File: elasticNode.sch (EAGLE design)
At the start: 136 parts, among them J1 FEMALE_HEADER_2X1, J2 JUMPER, J3 JUMPER, J5 FEMALE_HEADER_10X2, J6 USB_CONNMICRO_SMT, J7 USB_CONNMICRO_SMT, M1 SISS23DN, M2 SISS23DN, M3 SISS23DN, M4 SISS23DN, U1 AT90USB128, U10 LTC3419DFN, U11 PAC1720, U14 LTC3419DFN, U2 IS66WV51216EALL, U3 MRF24J40MA, U4 SPARTAN7-LX15, U5 ATMEGA32U4QFN, U6 SST26VF032BWDFN, U7 PAC1720, U8 PAC1720, U9 PAC1720, X1 8MHz, X2 50MHz, X3 32MHz, X4 100MHz, X5 8MHz

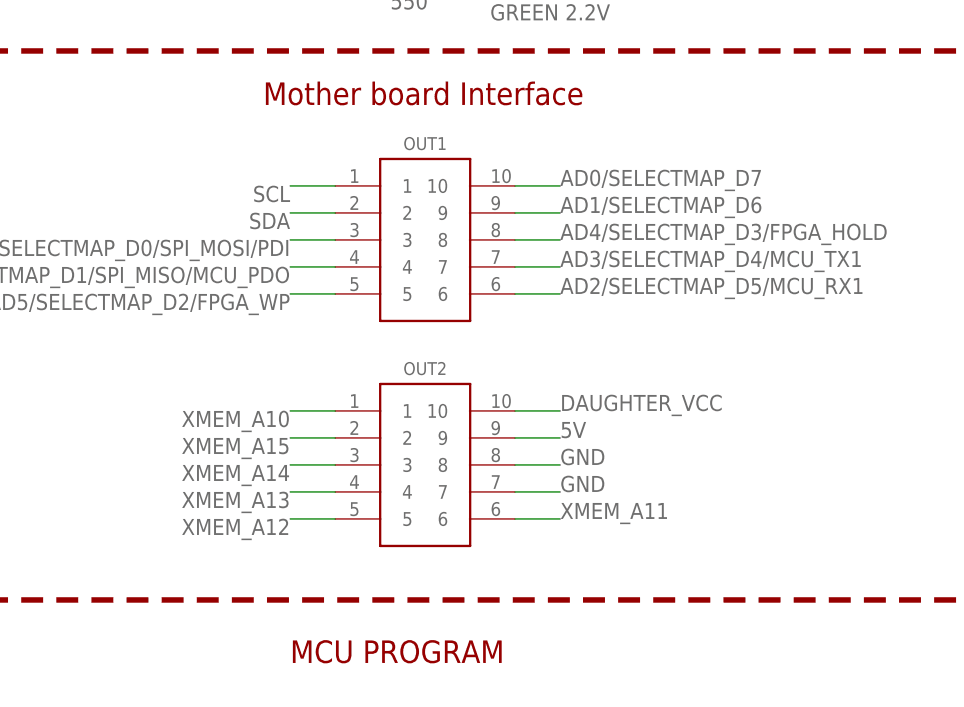
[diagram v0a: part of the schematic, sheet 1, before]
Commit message: Fixed all  DRC Errors and Warnings.
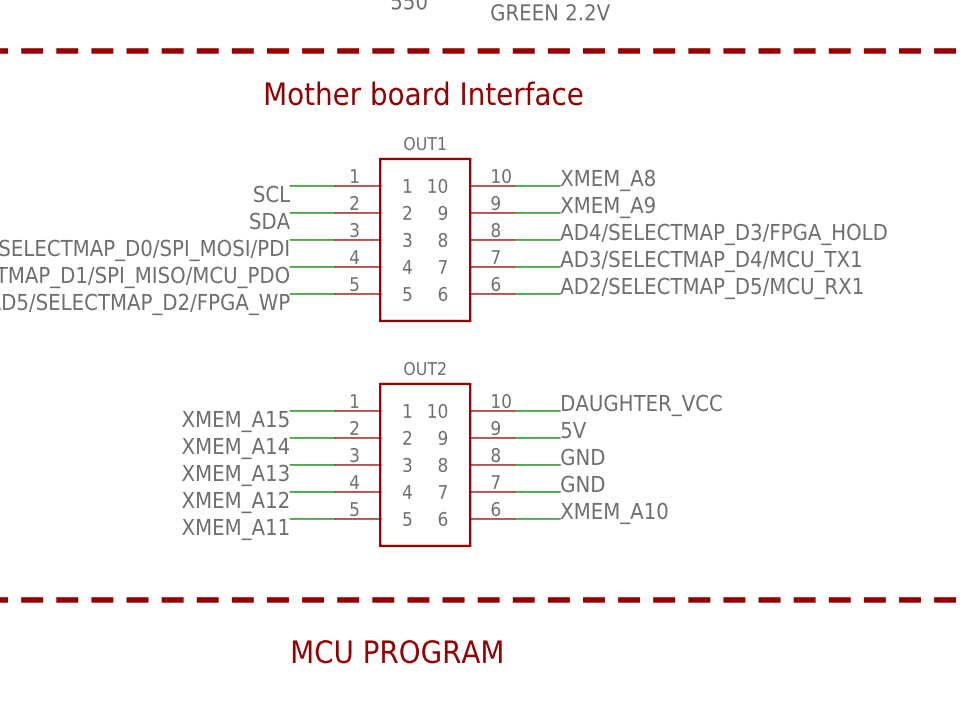
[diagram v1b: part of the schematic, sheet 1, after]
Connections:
- net AD0/SELECTMAP_D7: no longer OUT1.10
- net AD1/SELECTMAP_D6: no longer OUT1.9
- net XMEM_A10: now also OUT2.6; no longer OUT2.1
- net XMEM_A11: now also OUT2.5; no longer OUT2.6
- net XMEM_A12: now also OUT2.4; no longer OUT2.5
- net XMEM_A13: now also OUT2.3; no longer OUT2.4
- net XMEM_A14: now also OUT2.2; no longer OUT2.3
- net XMEM_A15: now also OUT2.1; no longer OUT2.2
- net XMEM_A8: now also OUT1.10
- net XMEM_A9: now also OUT1.9
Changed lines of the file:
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@@
 <setting verticaltext="up"/>
 </settings>
-<grid distance="1" unitdist="mm" unit="mm" style="lines" multiple="1" display="yes" altdistance="0.01" altunitdist="inch" altunit="inch"/>
+<grid distance="0.1" unitdist="inch" unit="inch" style="lines" multiple="1" display="no" altdistance="0.01" altunitdist="inch" altunit="inch"/>
 <layers>
 <layer number="1" name="Top" color="12" fill="1" visible="no" active="no"/>
@@
 <label x="-52" y="67" size="1.778" layer="95" rot="R90"/>
 </segment>
-<segment>
-<pinref part="OUT1" gate="G$1" pin="9"/>
-<wire x1="132" y1="43" x2="137" y2="43" width="0.1524" layer="91"/>
-<label x="137" y="43" size="1.778" layer="95"/>
-</segment>
 </net>
 <net name="AD3/SELECTMAP_D4/MCU_TX1" class="0">
@@
 </segment>
 <segment>
-<pinref part="OUT2" gate="G$1" pin="2"/>
-<wire x1="112" y1="18" x2="107" y2="18" width="0.1524" layer="91"/>
-<label x="107" y="18" size="1.778" layer="95" rot="R180"/>
+<pinref part="OUT2" gate="G$1" pin="1"/>
+<wire x1="112" y1="21" x2="107" y2="21" width="0.1524" layer="91"/>
+<label x="107" y="21" size="1.778" layer="95" rot="R180"/>
 </segment>
 </net>
@@
 <wire x1="-55" y1="51.16" x2="-55" y2="67" width="0.1524" layer="91"/>
 <label x="-55" y="67" size="1.778" layer="95" rot="R90"/>
-</segment>
-<segment>
-<pinref part="OUT1" gate="G$1" pin="10"/>
-<wire x1="132" y1="46" x2="137" y2="46" width="0.1524" layer="91"/>
-<label x="137" y="46" size="1.778" layer="95"/>
 </segment>
 </net>
@@
 <label x="-13" y="-10" size="1.778" layer="95"/>
 </segment>
+<segment>
+<pinref part="OUT1" gate="G$1" pin="10"/>
+<wire x1="132" y1="46" x2="137" y2="46" width="0.1524" layer="91"/>
+<label x="137" y="46" size="1.778" layer="95"/>
+</segment>
 </net>
 <net name="XMEM_A14" class="0">
@@
 </segment>
 <segment>
+<pinref part="OUT2" gate="G$1" pin="2"/>
+<wire x1="112" y1="18" x2="107" y2="18" width="0.1524" layer="91"/>
+<label x="107" y="18" size="1.778" layer="95" rot="R180"/>
+</segment>
+</net>
+<net name="XMEM_A13" class="0">
+<segment>
+<pinref part="U1" gate="G$1" pin="PC5(A13/OC.3B)"/>
+<wire x1="-26" y1="5" x2="-13" y2="5" width="0.1524" layer="91"/>
+<label x="-13" y="5" size="1.778" layer="95"/>
+</segment>
+<segment>
 <pinref part="OUT2" gate="G$1" pin="3"/>
 <wire x1="112" y1="15" x2="107" y2="15" width="0.1524" layer="91"/>
@@
 </segment>
 </net>
-<net name="XMEM_A13" class="0">
-<segment>
-<pinref part="U1" gate="G$1" pin="PC5(A13/OC.3B)"/>
-<wire x1="-26" y1="5" x2="-13" y2="5" width="0.1524" layer="91"/>
-<label x="-13" y="5" size="1.778" layer="95"/>
+<net name="XMEM_A12" class="0">
+<segment>
+<pinref part="U1" gate="G$1" pin="PC4(A12/OC.3C)"/>
+<wire x1="-26" y1="2" x2="-13" y2="2" width="0.1524" layer="91"/>
+<label x="-13" y="2" size="1.778" layer="95"/>
 </segment>
 <segment>
@@
 </segment>
 </net>
-<net name="XMEM_A12" class="0">
-<segment>
-<pinref part="U1" gate="G$1" pin="PC4(A12/OC.3C)"/>
-<wire x1="-26" y1="2" x2="-13" y2="2" width="0.1524" layer="91"/>
-<label x="-13" y="2" size="1.778" layer="95"/>
+<net name="XMEM_A11" class="0">
+<segment>
+<pinref part="U1" gate="G$1" pin="PC3(A11/T.3)"/>
+<wire x1="-26" y1="-1" x2="-13" y2="-1" width="0.1524" layer="91"/>
+<label x="-13" y="-1" size="1.778" layer="95"/>
 </segment>
 <segment>
@@
 </segment>
 </net>
-<net name="XMEM_A11" class="0">
-<segment>
-<pinref part="U1" gate="G$1" pin="PC3(A11/T.3)"/>
-<wire x1="-26" y1="-1" x2="-13" y2="-1" width="0.1524" layer="91"/>
-<label x="-13" y="-1" size="1.778" layer="95"/>
+<net name="XMEM_A10" class="0">
+<segment>
+<pinref part="U1" gate="G$1" pin="PC2(A10)"/>
+<wire x1="-26" y1="-4" x2="-13" y2="-4" width="0.1524" layer="91"/>
+<label x="-13" y="-4" size="1.778" layer="95"/>
 </segment>
 <segment>
@@
 </segment>
 </net>
-<net name="XMEM_A10" class="0">
-<segment>
-<pinref part="U1" gate="G$1" pin="PC2(A10)"/>
-<wire x1="-26" y1="-4" x2="-13" y2="-4" width="0.1524" layer="91"/>
-<label x="-13" y="-4" size="1.778" layer="95"/>
-</segment>
-<segment>
-<pinref part="OUT2" gate="G$1" pin="1"/>
-<wire x1="112" y1="21" x2="107" y2="21" width="0.1524" layer="91"/>
-<label x="107" y="21" size="1.778" layer="95" rot="R180"/>
-</segment>
-</net>
 <net name="XMEM_A9" class="0">
 <segment>
@@
 <label x="-13" y="-7" size="1.778" layer="95"/>
 </segment>
-</net>
+<segment>
+<pinref part="OUT1" gate="G$1" pin="9"/>
+<wire x1="132" y1="43" x2="137" y2="43" width="0.1524" layer="91"/>
+<label x="137" y="43" size="1.778" layer="95"/>
+</segment>
+</net>

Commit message: Add JTAG Header
Checked the schematic diagram again.
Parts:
- removed C36, C40: 4.7u, passive:CAPACITOR0805
- removed D12: GREEN 2.2V, opto:LED
- removed L6: 3.3uH, passive:INDUCTOR
- removed MCU_PROGRAM, MON_PROGRAM: ISP_CONN_6PIN, connectors:ISP_CONN_6PIN
- removed OUT1, OUT2: FEMALE_HEADER_5X2, connectors:FEMALE_HEADER_5X2
- removed R50, R51: 550, passive:RESISTOR
- removed R52, R53: 22, passive:RESISTOR
- removed R54: 15k, passive:RESISTOR
- removed TP7: TEST_POINTTHT, connectors:TEST_POINTTHT
- removed U14: LTC3419DFN, power:LTC3419DFN
- added C18, C26: 4.7u, passive:CAPACITOR0805
- added D10: RED, opto:LED
- added J10, J8: USB_CONNMICRO_SMT, connectors:USB_CONNMICRO_SMT
- added J11: JTAG_CONN_6PINSMT, connectors:JTAG_CONN_6PINSMT
- added J4: FEMALE_HEADER_2X1, connectors:FEMALE_HEADER_2X1
- added J9: FEMALE_HEADER_10X2, connectors:FEMALE_HEADER_10X2
- added L3: 3.3uH, passive:INDUCTOR
- added R40: 750, passive:RESISTOR
- added R44: 20k, passive:RESISTOR
- added R45: 1k5, passive:RESISTOR
- added R46: 6k8, passive:RESISTOR
- added R48: 270, passive:RESISTOR
- added TP5: TEST_POINTTHT, connectors:TEST_POINTTHT
- added U12: LTC3419DFN, power:LTC3419DFN
- C10, C29, C30: value 4.7u -> 0.47u
- C12: value 10u -> 47u; device passive:CAPACITOR0805 -> passive:CAPACITOR1210
- C13: value 0.47u -> 4.7
- C15, C28: value 10u -> 0.47u
- C17: value 22u -> 100u; device passive:CAPACITOR0805 -> passive:CAPACITOR1210
- C19, C27: value 22u -> 4.7u
- C20: value 0.47u -> 4.7u
- C31, C32: value 0.47u -> 10u
- C33: value 0.47u -> 22u
- C34: value 100u -> 22u; device passive:CAPACITOR1210 -> passive:CAPACITOR0805
- C35: value 4.7u -> 22u
- C4: value 100u -> 10u; device passive:CAPACITOR1210 -> passive:CAPACITOR0805
- C5: value 47u -> 20p; device passive:CAPACITOR1210 -> passive:CAPACITOR0805
- C7: value 4.7u -> 100u
- C8: value 4.7 -> 4.7u; device passive:CAPACITOR0805 -> passive:CAPACITOR1210
- C9: value 20p -> 4.7u
- D11: value GREEN 2.2V -> RED
- D5: value RED 1.8V 2mA -> GREEN 2.2V
- D6: value RED -> GREEN 2.2V
- D7: value RED -> RED 1.8V 2mA
- J1: value FEMALE_HEADER_2X1 -> FEMALE_HEADER_5X2; device connectors:FEMALE_HEADER_2X1 -> connectors:FEMALE_HEADER_5X2
- J2: value JUMPER -> FEMALE_HEADER_5X2; device connectors:JUMPER -> connectors:FEMALE_HEADER_5X2
- J3: value JUMPER -> ISP_CONN_6PIN; device connectors:JUMPER -> connectors:ISP_CONN_6PIN; SPICEPREFIX (none) -> X
- J5: value FEMALE_HEADER_10X2 -> JUMPER; device connectors:FEMALE_HEADER_10X2 -> connectors:JUMPER
- J6: value USB_CONNMICRO_SMT -> ISP_CONN_6PIN; device connectors:USB_CONNMICRO_SMT -> connectors:ISP_CONN_6PIN
- J7: value USB_CONNMICRO_SMT -> JUMPER; device connectors:USB_CONNMICRO_SMT -> connectors:JUMPER
- R1, R2: value 22 -> 550
- R10: value 4.7k -> 550
- R11: value 750 -> 550
- R12: value 750 -> 15k
- R13: value 750 -> 0
- R14: value 750 -> 22
- R15: value 15k -> 22
- R17: value 2.4k -> 15k
- R18, R19: value 2.4k -> 750
- R20: value 0.8 -> 750
- R21: value .8 -> 4.7k
- R22: value .8 -> 750
- R23: value 0.8 -> 2.4k
- R24, R25: value .8 -> 2.4k
- R26: value 100 -> 2.4k
- R27: value 2000 -> 15k
- R28: value 300 -> 1.5k
- R29: value 0 -> 1.5k
- R3: value 2.4k -> 550
- R30: value 15k -> 0.8
- R31: value 10k -> .8
- R32: value 6k8 -> 0.8
- R33: value 270 -> .8
- R34: value 10k -> 100
- R35: value 750 -> 2000
- R36: value 0.15 -> .8
- R37: value 1k5 -> .8
- R38: value 6k8 -> 0.15
- R39: value 2.4k -> .8
- R4: value 10k -> 550
- R41: value 1.5k -> 300
- R42: value 1.5k -> 6k8
- R43: value .8 -> 10k
- R47: value 20k -> 10k
- R5, R6: value 550 -> 22
- R7: value 550 -> 2.4k
- R8: value 550 -> 15k
- R9: value 15k -> 10k
- S2: value SPST_BUTTON2PIN_SMT -> SPST_DIP_4; device connectors:SPST_BUTTON2PIN_SMT -> connectors:SPST_DIP_4
- S3: value SPST_DIP_4 -> SPST_BUTTON2PIN_SMT; device connectors:SPST_DIP_4 -> connectors:SPST_BUTTON2PIN_SMT
- U10: value LTC3419DFN -> PAC1720; device power:LTC3419DFN -> sensors:PAC1720
- U11: value PAC1720 -> LTC3419DFN; device sensors:PAC1720 -> power:LTC3419DFN
- U2: value IS66WV51216EALL -> MRF24J40MA; device ic:IS66WV51216EALL -> wireless:MRF24J40MA
- U3: value MRF24J40MA -> ATMEGA32U4QFN; device wireless:MRF24J40MA -> ic:ATMEGA32U4QFN
- U4: value SPARTAN7-LX15 -> IS66WV51216EALL; device fpga:SPARTAN7-LX15 -> ic:IS66WV51216EALL
- U5: value ATMEGA32U4QFN -> SPARTAN7-LX15; device ic:ATMEGA32U4QFN -> fpga:SPARTAN7-LX15
- X2: value 50MHz -> 8MHz; device passive:OSCILLATOR3.2X2.5 -> passive:QUARTZ
- X3: value 32MHz -> 100MHz
- X4: value 100MHz -> 50MHz
- X5: value 8MHz -> 32MHz; device passive:QUARTZ -> passive:OSCILLATOR3.2X2.5
- renumbered C37 to C21, C38 to C22, C39 to C23, TP8 to TP4
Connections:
- net 1V: now also C34.P$1, L2.P$2, R39.2, R43.2, U10.SENSE2+; no longer C17.P$1, L1.P$2, R22.2, R31.2, U9.SENSE2+
- net 1V8: now also C35.P$2, L3.P$1, R30.2, R37.2, R44.1, TP3.>NAME, U10.SENSE1+; no longer C19.P$2, L2.P$1, R23.2, R25.2, R47.1, TP7.>NAME, U9.SENSE1+
- net 3V3: now also C33.P$1, C4.P$1, J3.VCC, J6.VCC, L1.P$1, R12.1, R13.2, R16.1, R17.1, R26.1, R28.2, R31.2, R32.2, R33.2, R36.2, U10.VDD, U12.RUN2, U3.AVCC, U3.UCAP, U3.VCC, U9.SENSE1+; no longer C12.P$1, C27.P$1, L6.P$1, MCU_PROGRAM.VCC, MON_PROGRAM.VCC, R19.1, R20.2, R21.2, R24.2, R30.1, R38.2, R39.1, R41.2, R43.2, R54.1, U10.RUN2, U11.SENSE1+, U11.VDD, U5.AVCC, U5.UCAP, U5.VCC
- net 5V: now also C31.P$1, C32.P$1, J2.9, R38.2, U11.MODE, U11.RUN1, U11.VIN, U12.MODE, U12.RUN1, U12.VIN, U9.SENSE2+; no longer C15.P$1, C28.P$1, OUT2.9, R36.2, U10.MODE, U10.RUN1, U10.VIN, U11.SENSE2+, U14.MODE, U14.RUN1, U14.VIN
- net AD0/SELECTMAP_D7: now also U5.IO_L5N_T0_D07_14; no longer U4.IO_L5N_T0_D07_14
- net AD1/SELECTMAP_D6: now also U5.IO_L5P_T0_D06_14; no longer U4.IO_L5P_T0_D06_14
- net AD2/SELECTMAP_D5/MCU_RX1: now also J1.6, U5.IO_L4N_T0_D05_14; no longer OUT1.6, U4.IO_L4N_T0_D05_14
- net AD3/SELECTMAP_D4/MCU_TX1: now also J1.7, U5.IO_L4P_T0_D04_14; no longer OUT1.7, U4.IO_L4P_T0_D04_14
- net AD4/SELECTMAP_D3/FPGA_HOLD: now also J1.8, U5.IO_L2N_T0_D03_14; no longer OUT1.8, U4.IO_L2N_T0_D03_14
- net AD5/SELECTMAP_D2/FPGA_WP: now also J1.5, U5.IO_L2P_T0_D02_14; no longer OUT1.5, U4.IO_L2P_T0_D02_14
- net AD6/SELECTMAP_D1/SPI_MISO/MCU_PDO: now also J1.4, J3.MISO, U2.SDO, U5.IO_L1N_T0_D01_DIN_14; no longer MCU_PROGRAM.MISO, OUT1.4, U3.SDO, U4.IO_L1N_T0_D01_DIN_14
- net AD7/SELECTMAP_D0/SPI_MOSI/PDI: now also J1.3, J3.MOSI, U2.SDI, U5.IO_L1P_T0_D00_MOSI_14; no longer MCU_PROGRAM.MOSI, OUT1.3, U3.SDI, U4.IO_L1P_T0_D00_MOSI_14
- net ALE/HWB: now also J5.1, R9.2, U5.IO_L12P_T1_MRCC_14; no longer J2.1, R4.2, U4.IO_L12P_T1_MRCC_14
- net DAUGHTER_VCC: now also J2.10, R31.1; no longer OUT2.10, R24.1
- net FPGA_DONE: now also U5.DONE_0; no longer U4.DONE_0
- net FPGA_GPIO_0: now also J9.1, U5.IO_L14N_T2_SRCC_14; no longer J5.1, U4.IO_L14N_T2_SRCC_14
- net FPGA_GPIO_1: now also J9.20, U5.IO_L18N_T2_D27_14; no longer J5.20, U4.IO_L16N_T2_D31_14
- net FPGA_GPIO_10: now also J9.15, U5.IO_L21N_T3_DQS_D22_14; no longer J5.15, U4.IO_L22P_T3_D21_14
- net FPGA_GPIO_11: now also J9.6, U5.IO_L16N_T2_D31_14; no longer J5.6, U4.IO_L17N_T2_D29_14
- net FPGA_GPIO_12: now also J9.14, U5.IO_L21P_T3_DQS_14; no longer J5.14, U4.IO_L23N_T3_D18_14
- net FPGA_GPIO_13: now also J9.7, U5.IO_L20N_T3_D23_14; no longer J5.7, U4.IO_L17P_T2_D30_14
- net FPGA_GPIO_14: now also J9.8, U5.IO_L22N_T3_D20_14; no longer J5.8, U4.IO_L19N_T3_D25_VREF_14
- net FPGA_GPIO_15: now also J9.13, U5.IO_L22P_T3_D21_14; no longer J5.13, U4.IO_L24N_T3_D16_14
- net FPGA_GPIO_16: now also J9.9, U5.IO_L23N_T3_D18_14; no longer J5.9, U4.IO_L19P_T3_D26_14
- net FPGA_GPIO_17: now also J9.12, U5.IO_L24N_T3_D16_14; no longer J5.12, U4.IO_L23P_T3_D19_14
- net FPGA_GPIO_18: now also J9.10, U5.IO_L23P_T3_D19_14; no longer J5.10, U4.IO_L15N_T2_DQS_DOUT_CSO_B_14
- net FPGA_GPIO_19: now also J9.11, U5.IO_L24P_T3_D17_14; no longer J5.11, U4.IO_L24P_T3_D17_14
- net FPGA_GPIO_2: now also J9.2, U5.IO_L14P_T2_SRCC_14; no longer J5.2, U4.IO_L14P_T2_SRCC_14
- net FPGA_GPIO_3: now also J9.19, U5.IO_L18P_T2_D28_14; no longer J5.19, U4.IO_L21N_T3_DQS_D22_14
- net FPGA_GPIO_4: now also J9.3, U5.IO_L13N_T2_MRCC_14; no longer J5.3, U4.IO_L13N_T2_MRCC_14
- net FPGA_GPIO_5: now also J9.18, U5.IO_L17N_T2_D29_14; no longer J5.18, U4.IO_L20N_T3_D23_14
- net FPGA_GPIO_6: now also J9.4, U5.IO_L17P_T2_D30_14; no longer J5.4, U4.IO_L18P_T2_D28_14
- net FPGA_GPIO_7: now also J9.17, U5.IO_L19N_T3_D25_VREF_14; no longer J5.17, U4.IO_L21P_T3_DQS_14
- net FPGA_GPIO_8: now also J9.5, U5.IO_L19P_T3_D26_14; no longer J5.5, U4.IO_L18N_T2_D27_14
- net FPGA_GPIO_9: now also J9.16, U5.IO_L15N_T2_DQS_DOUT_CSO_B_14; no longer J5.16, U4.IO_L22N_T3_D20_14
- net FPGA_LED0: now also R18.1, U5.IO_0_14; no longer R11.1, U4.IO_0_14
- net FPGA_LED1: now also R19.1, U5.IO_L3P_T0_DQS_PUDC_B_14; no longer R12.1, U4.IO_L3P_T0_DQS_PUDC_B_14
- net FPGA_LED2: now also R20.1, U5.IO_L3N_T0_DQS_EMCCLK_14; no longer R13.1, U4.IO_L3N_T0_DQS_EMCCLK_14
- net FPGA_LED3: now also R22.1, U5.IO_L6N_T0_D08_VREF_14; no longer R14.1, U4.IO_L6N_T0_D08_VREF_14
- net FPGA_RESET: now also R27.1, S3.3, U5.PROGRAM_B_0; no longer R15.1, S2.3, U4.PROGRAM_B_0
- net FPGA_VCCAUX: now also C12.P$1, C13.P$1, C15.P$1, C16.P$1, R21.2, R25.1, R27.2, U5.CFGBVS_0, U5.VCCAUX, X4.EN, X4.VS+, X5.EN, X5.VS+; no longer C11.P$1, C20.P$1, C5.P$1, C8.P$1, R10.2, R15.2, R16.1, U4.CFGBVS_0, U4.VCCAUX, X2.EN, X2.VS+, X3.EN, X3.VS+
- net FPGA_VCCAUX_MON: now also R37.1, U10.SENSE1-; no longer R25.1, U9.SENSE1-
- net FPGA_VCCINT: now also C11.P$1, C8.P$1, C9.P$1, U5.VCCBRAM, U5.VCCINT; no longer C13.P$1, C16.P$1, C4.P$1, U4.VCCBRAM, U4.VCCINT
- net FPGA_VCCINT_MON: now also R39.1, U10.SENSE2-; no longer R22.1, U9.SENSE2-
- net FPGA_VCCIO: now also C17.P$1, C18.P$1, C19.P$1, C20.P$1, J11.REF, R23.1, R24.1, U5.VCCO_0, U5.VCCO_14; no longer C34.P$1, C35.P$1, C36.P$1, C40.P$1, R17.1, R18.1, U4.VCCO_0, U4.VCCO_14
- net FPGA_VCCIO_MON: now also R32.1; no longer R20.1
- net GND: now also C18.P$2, C19.P$2, C26.P$2, C35.P$1, D10.2, D9.2, J10.GND, J11.GND, J2.7, J2.8, J3.GND, J5.2, J7.2, J8.GND, R40.1, R41.1, R45.2, R46.2, R47.1, R48.1, S2.1Y, S2.2Y, S2.3Y, S2.4Y, S3.1, TP5.>NAME, U12.GND, U2.GND, U3.UGND, U4.GND@1, U4.GND@2, U5.DXN_0, U5.DXP_0, U5.IO_L15P_T2_DQS_RDWR_B_14, U5.IO_L16P_T2_CSI_B_14, X5.GND; no longer C19.P$1, C35.P$2, C36.P$2, C40.P$2, D11.2, D12.2, J2.2, J3.2, J7.GND, MCU_PROGRAM.GND, MON_PROGRAM.GND, OUT2.7, OUT2.8, R26.1, R27.1, R28.1, R32.2, R33.1, R37.2, S2.1, S3.1Y, S3.2Y, S3.3Y, S3.4Y, TP3.>NAME, U14.GND, U2.GND@1, U2.GND@2, U4.DXN_0, U4.DXP_0, U4.GND, U4.IO_L15P_T2_DQS_RDWR_B_14, U4.IO_L16P_T2_CSI_B_14, U5.UGND, X2.GND
- net INIT_B: now also R21.1, U5.INIT_B_0; no longer R10.1, U4.INIT_B_0
- net JTAG_TCK: now also J11.TCK, U5.TCK_0; no longer U4.TCK_0
- net JTAG_TDI: now also J11.TDI, U5.TDI_0; no longer U4.TDI_0
- net JTAG_TDO: now also J11.TDO, U5.TDO_0; no longer U4.TDO_0
- net JTAG_TMS: now also J11.TMS, U5.TMS_0; no longer U4.TMS_0
- net MCU_LED0: now also R1.1; no longer R5.1
- net MCU_LED1: now also R2.1; no longer R6.1
- net MCU_LED2: now also R3.1; no longer R7.1
- net MCU_LED3: now also R4.1; no longer R8.1
- net MCU_RESET: now also J3.RST, R8.1; no longer MCU_PROGRAM.RST, R9.1
- net MCU_RX: now also J4.2; no longer J1.2
- net MCU_TX: now also J4.1; no longer J1.1
- net MCU_VCC: now also R33.1, R7.1, R8.2, R9.1; no longer R21.1, R3.1, R4.1, R9.2
- net MODE0: now also R23.2, S2.1X, U5.M0_0; no longer R18.2, S3.1X, U4.M0_0
- net MODE1: now also R24.2, S2.2X, U5.M1_0; no longer R17.2, S3.2X, U4.M1_0
- net MODE2: now also R25.2, S2.3X, U5.M2_0; no longer R16.2, S3.3X, U4.M2_0
- net MONITORING: now also R16.2, S2.4X, U3.PE6(INT6/AIN0); no longer R39.2, S3.4X, U5.PE6(INT6/AIN0)
- net MON_HWB: now also J7.1, R12.2, U3.PE2(HWB); no longer J3.1, R30.2, U5.PE2(HWB)
- net MON_LED0: now also R10.1, U3.PD2(RXD1/INT2); no longer R50.1, U5.PD2(RXD1/INT2)
- net MON_LED1: now also R11.1, U3.PD3(TXD1/INT3); no longer R51.1, U5.PD3(TXD1/INT3)
- net MON_MISO: now also J6.MISO, U3.PB3(PDO/PCINT3/MISO); no longer MON_PROGRAM.MISO, U5.PB3(PDO/PCINT3/MISO)
- net MON_MOSI: now also J6.MOSI, U3.PB2(PDI/PCINT2/MOSI); no longer MON_PROGRAM.MOSI, U5.PB2(PDI/PCINT2/MOSI)
- net MON_RESET: now also J6.RST, R17.2, U3._RESET; no longer MON_PROGRAM.RST, R54.2, U5._RESET
- net MON_SCK: now also J6.SCK, U3.PB1(PCINT1/SCL); no longer MON_PROGRAM.SCK, U5.PB1(PCINT1/SCL)
- net MON_USB_D+: now also R15.1, U3.D+; no longer R53.1, U5.D+
- net MON_USB_D-: now also R14.1, U3.D-; no longer R52.1, U5.D-
- net MON_USB_VCC: now also J8.VCC, U3.VBUS; no longer J7.VCC, U5.VBUS
- net N$10: now also R6.2; no longer R1.2
- net N$11: now also R40.2, U9.ADDR_SEL; no longer R35.2, U11.ADDR_SEL
- net N$12: now also R34.2; no longer R26.2
- net N$13: now also R4.2; no longer R8.2
- net N$14: now also R35.2; no longer R27.2
- net N$15: now also R3.2; no longer R7.2
- net N$16: now also D6.1, R11.2; no longer D12.1, R51.2
- net N$17: now also D5.1, R10.2; no longer D11.1, R50.2
- net N$18: now also C5.P$1, U3.XTAL1, X2.P$2; no longer C9.P$1, U5.XTAL1, X5.P$2
- net N$19: now also J8.D-, R14.2; no longer J7.D-, R52.2
- net N$2: now also R43.1, R46.1, U12.VFB1; no longer R31.1, R32.1, U10.VFB1
- net N$20: now also U3.XTAL2, X2.P$1; no longer U5.XTAL2, X5.P$1
- net N$21: now also R13.1, U3.UVCC; no longer R29.1, U5.UVCC
- net N$22: now also L2.P$1, U12.SW1; no longer L1.P$1, U10.SW1
- net N$23: now also R2.2; no longer R6.2
- net N$24: now also R1.2; no longer R5.2
- net N$25: now also D10.1, R22.2; no longer D8.1, R14.2
- net N$26: now also L3.P$2, U12.SW2; no longer L2.P$2, U10.SW2
- net N$27: now also D9.1, R20.2; no longer D7.1, R13.2
- net N$28: now also D11.2, R48.2; no longer D9.2, R33.2
- net N$29: now also D8.1, R19.2; no longer D6.1, R12.2
- net N$3: now also R5.2; no longer R2.2
- net N$30: now also D7.1, R18.2; no longer D5.1, R11.2
- net N$5: now also J8.D+, R15.2; no longer J7.D+, R53.2
- net N$53: now also R42.1, R45.1, U11.VFB1; no longer R37.1, R38.1, U14.VFB1
- net N$55: now also L1.P$2, U11.SW1; no longer L6.P$2, U14.SW1
- net N$7: now also R44.2, U12.VFB2; no longer R34.2, U10.VFB2
- net N$9: now also R41.2, U10.ADDR_SEL; no longer R28.2, U9.ADDR_SEL
- net OSC_100: now also U5.IO_L12P_T1_MRCC_34, X3.OUTPUT; no longer U4.IO_L12P_T1_MRCC_34, X4.OUTPUT
- net OSC_32: now also U5.IO_L13P_T2_MRCC_14, X5.OUTPUT; no longer U4.IO_L13P_T2_MRCC_14, X3.OUTPUT
- net OSC_50: now also U5.IO_L12N_T1_MRCC_14, X4.OUTPUT; no longer U4.IO_L12N_T1_MRCC_14, X2.OUTPUT
- net SCL: now also J1.1, R28.1, U10.SMCLK, U3.PD0(OC0B/SCL/INT0); no longer OUT1.1, R41.1, U11.SMCLK, U5.PD0(OC0B/SCL/INT0)
- net SDA: now also J1.2, R29.1, U10.SMDATA, U3.PD1(SDA/INT1); no longer OUT1.2, R42.1, U11.SMDATA, U5.PD1(SDA/INT1)
- net SPI_CS: now also R26.2, U5.IO_L6P_T0_FCS_B_14; no longer R19.2, U4.IO_L6P_T0_FCS_B_14
- net SPI_SCK/CCLK: now also J3.SCK, U2.SCK, U5.CCLK_0; no longer MCU_PROGRAM.SCK, U3.SCK, U4.CCLK_0
- net SRAM_A0: now also U4.A0, U5.IO_L3P_T0_DQS_34; no longer U2.A0, U4.IO_L3P_T0_DQS_34
- net SRAM_A1: now also U4.A1, U5.IO_L5P_T0_34; no longer U2.A1, U4.IO_L5P_T0_34
- net SRAM_A10: now also U4.A10, U5.IO_L23P_T3_34; no longer U2.A10, U4.IO_L23P_T3_34
- net SRAM_A11: now also U4.A11, U5.IO_L20N_T3_34; no longer U2.A11, U4.IO_L20N_T3_34
- net SRAM_A12: now also U4.A12, U5.IO_L24P_T3_34; no longer U2.A12, U4.IO_L24P_T3_34
- net SRAM_A13: now also U4.A13, U5.IO_L21P_T3_DQS_34; no longer U2.A13, U4.IO_L21P_T3_DQS_34
- net SRAM_A14: now also U4.A14, U5.IO_L21N_T3_DQS_34; no longer U2.A14, U4.IO_L21N_T3_DQS_34
- net SRAM_A15: now also U4.A15, U5.IO_L20P_T3_34; no longer U2.A15, U4.IO_L20P_T3_34
- net SRAM_A16: now also U4.A16, U5.IO_L17P_T2_34; no longer U2.A16, U4.IO_L17P_T2_34
- net SRAM_A17: now also U4.A17, U5.IO_L24N_T3_34; no longer U2.A17, U4.IO_L24N_T3_34
- net SRAM_A18: now also U4.A18, U5.IO_L19N_T3_VREF_34; no longer U2.A18, U4.IO_L19N_T3_VREF_34
- net SRAM_A2: now also U4.A2, U5.IO_L4P_T0_34; no longer U2.A2, U4.IO_L4P_T0_34
- net SRAM_A3: now also U4.A3, U5.IO_0_34; no longer U2.A3, U4.IO_0_34
- net SRAM_A4: now also U4.A4, U5.IO_L4N_T0_34; no longer U2.A4, U4.IO_L4N_T0_34
- net SRAM_A5: now also U4.A5, U5.IO_L2P_T0_34; no longer U2.A5, U4.IO_L2P_T0_34
- net SRAM_A6: now also U4.A6, U5.IO_L2N_T0_34; no longer U2.A6, U4.IO_L2N_T0_34
- net SRAM_A7: now also U4.A7, U5.IO_L3N_T0_DQS_34; no longer U2.A7, U4.IO_L3N_T0_DQS_34
- net SRAM_A8: now also U4.A8, U5.IO_L19P_T3_34; no longer U2.A8, U4.IO_L19P_T3_34
- net SRAM_A9: now also U4.A9, U5.IO_L23N_T3_34; no longer U2.A9, U4.IO_L23N_T3_34
- net SRAM_CS: now also U4.CS1#, U5.IO_L1N_T0_34; no longer U2.CS1#, U4.IO_L1N_T0_34
- net SRAM_D0: now also U4.I/O0, U5.IO_L6N_T0_VREF_34; no longer U2.I/O0, U4.IO_L6N_T0_VREF_34
- net SRAM_D1: now also U4.I/O1, U5.IO_L10N_T1_34; no longer U2.I/O1, U4.IO_L10N_T1_34
- net SRAM_D10: now also U4.I/O10, U5.IO_L18N_T2_34; no longer U2.I/O10, U4.IO_L18N_T2_34
- net SRAM_D11: now also U4.I/O11, U5.IO_L22N_T3_34; no longer U2.I/O11, U4.IO_L22N_T3_34
- net SRAM_D12: now also U4.I/O12, U5.IO_L15N_T2_DQS_34; no longer U2.I/O12, U4.IO_L15N_T2_DQS_34
- net SRAM_D13: now also U4.I/O13, U5.IO_L14N_T2_SRCC_34; no longer U2.I/O13, U4.IO_L14N_T2_SRCC_34
- net SRAM_D14: now also U4.I/O14, U5.IO_L9P_T1_DQS_34; no longer U2.I/O14, U4.IO_L9P_T1_DQS_34
- net SRAM_D15: now also U4.I/O15, U5.IO_L9N_T1_DQS_34; no longer U2.I/O15, U4.IO_L9N_T1_DQS_34
- net SRAM_D2: now also U4.I/O2, U5.IO_L1P_T0_34; no longer U2.I/O2, U4.IO_L1P_T0_34
- net SRAM_D3: now also U4.I/O3, U5.IO_L10P_T1_34; no longer U2.I/O3, U4.IO_L10P_T1_34
- net SRAM_D4: now also U4.I/O4, U5.IO_L8N_T1_34; no longer U2.I/O4, U4.IO_L8N_T1_34
- net SRAM_D5: now also U4.I/O5, U5.IO_L8P_T1_34; no longer U2.I/O5, U4.IO_L8P_T1_34
- net SRAM_D6: now also U4.I/O6, U5.IO_L14P_T2_SRCC_34; no longer U2.I/O6, U4.IO_L14P_T2_SRCC_34
- net SRAM_D7: now also U4.I/O7, U5.IO_L13N_T2_MRCC_34; no longer U2.I/O7, U4.IO_L13N_T2_MRCC_34
- net SRAM_D8: now also U4.I/O8, U5.IO_L18P_T2_34; no longer U2.I/O8, U4.IO_L18P_T2_34
- net SRAM_D9: now also U4.I/O9, U5.IO_L22P_T3_34; no longer U2.I/O9, U4.IO_L22P_T3_34
- net SRAM_LB: now also U4.LB#, U5.IO_L11P_T1_SRCC_34; no longer U2.LB#, U4.IO_L11P_T1_SRCC_34
- net SRAM_OE: now also U4.OE#, U5.IO_L5N_T0_34; no longer U2.OE#, U4.IO_L5N_T0_34
- net SRAM_UB: now also U4.UB#, U5.IO_L11N_T1_SRCC_34; no longer U2.UB#, U4.IO_L11N_T1_SRCC_34
- net SRAM_VDD: now also C26.P$1, C27.P$1, C28.P$1, U4.VDD@1, U4.VDD@2, U5.VCCO_34, X3.EN, X3.VS+; no longer C31.P$1, C32.P$1, C33.P$1, U2.VDD@1, U2.VDD@2, U4.VCCO_34, X4.EN, X4.VS+
- net SRAM_VDD_MON: now also R30.1; no longer R23.1
- net SRAM_WE: now also U4.WE#, U5.IO_L13P_T2_MRCC_34; no longer U2.WE#, U4.IO_L13P_T2_MRCC_34
- net UID: now also J10.UID; no longer J6.UID
- net USBD+: now also J10.D+, R6.1; no longer J6.D+, R1.1
- net USBD-: now also J10.D-, R5.1; no longer J6.D-, R2.1
- net USB_VCC_RAW: now also D11.1, J10.VCC, R38.1, U9.SENSE2-; no longer D9.1, J6.VCC, R36.1, U11.SENSE2-
- net WIRELESS_CS: now also R7.2, U2._CS; no longer R3.2, U3._CS
- net WIRELESS_INT: now also U2.INT; no longer U3.INT
- net WIRELESS_RESET: now also U2._RESET; no longer U3._RESET
- net WIRELESS_VCC: now also R36.1, U2.VI, U9.SENSE1-; no longer R43.1, U11.SENSE1-, U3.VI
- net WIRELESS_WAKE: now also U2.WAKE; no longer U3.WAKE
- net XMEM_A10: now also J2.6, U5.IO_L10N_T1_D15_14; no longer OUT2.6, U4.IO_L10N_T1_D15_14
- net XMEM_A11: now also J2.5, U5.IO_L7N_T1_D10_14; no longer OUT2.5, U4.IO_L7N_T1_D10_14
- net XMEM_A12: now also J2.4, U5.IO_L9N_T1_DQS_D13_14; no longer OUT2.4, U4.IO_L9N_T1_DQS_D13_14
- net XMEM_A13: now also J2.3, U5.IO_L10P_T1_D14_14; no longer OUT2.3, U4.IO_L10P_T1_D14_14
- net XMEM_A14: now also J2.2, U5.IO_L7P_T1_D09_14; no longer OUT2.2, U4.IO_L7P_T1_D09_14
- net XMEM_A15: now also J2.1, U5.IO_L9P_T1_DQS_14; no longer OUT2.1, U4.IO_L9P_T1_DQS_14
- net XMEM_A8: now also J1.10, U5.IO_L8N_T1_D12_14; no longer OUT1.10, U4.IO_L8N_T1_D12_14
- net XMEM_A9: now also J1.9, U5.IO_L8P_T1_D11_14; no longer OUT1.9, U4.IO_L8P_T1_D11_14
- net XMEM_RD: now also U5.IO_L11P_T1_SRCC_14; no longer U4.IO_L11P_T1_SRCC_14
- net XMEM_WR: now also U5.IO_L11N_T1_SRCC_14; no longer U4.IO_L11N_T1_SRCC_14
